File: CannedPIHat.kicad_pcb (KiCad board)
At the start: 4 copper layers, 65 x 57.2 mm, 103 parts, among them IC1 TPS56428DDA, IC2 LM1117MPX-3.3, IC3 STM32G474RET6, IC4 TJA1021TK_20_C,118, IC6 SN74LVC1G66QDCKRQ1, IC7 SN74LVC1G66QDCKRQ1, IC8 SN74LVC1G66QDCKRQ1, J1 Barrel_Jack_Switch, J2 09562627813, J5 20021511-00014T4LF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

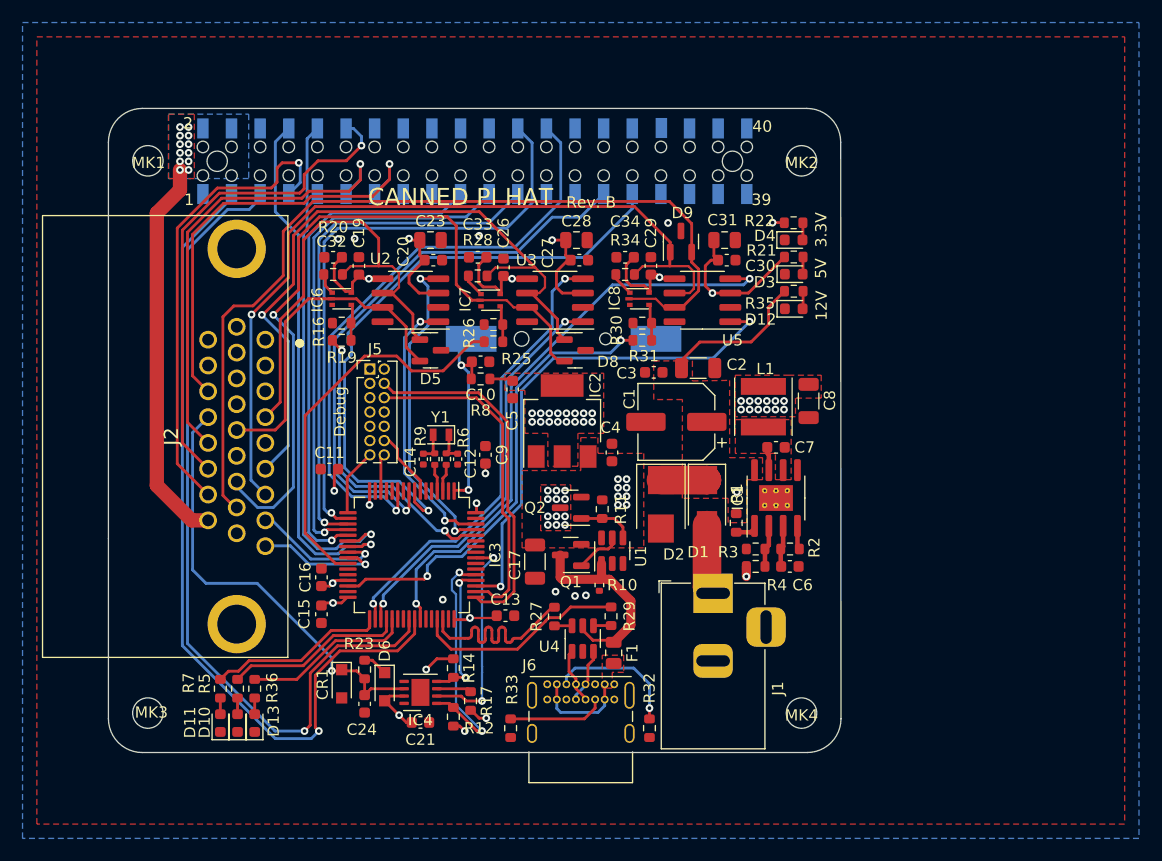
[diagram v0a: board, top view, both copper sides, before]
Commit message: Update to Rev C.
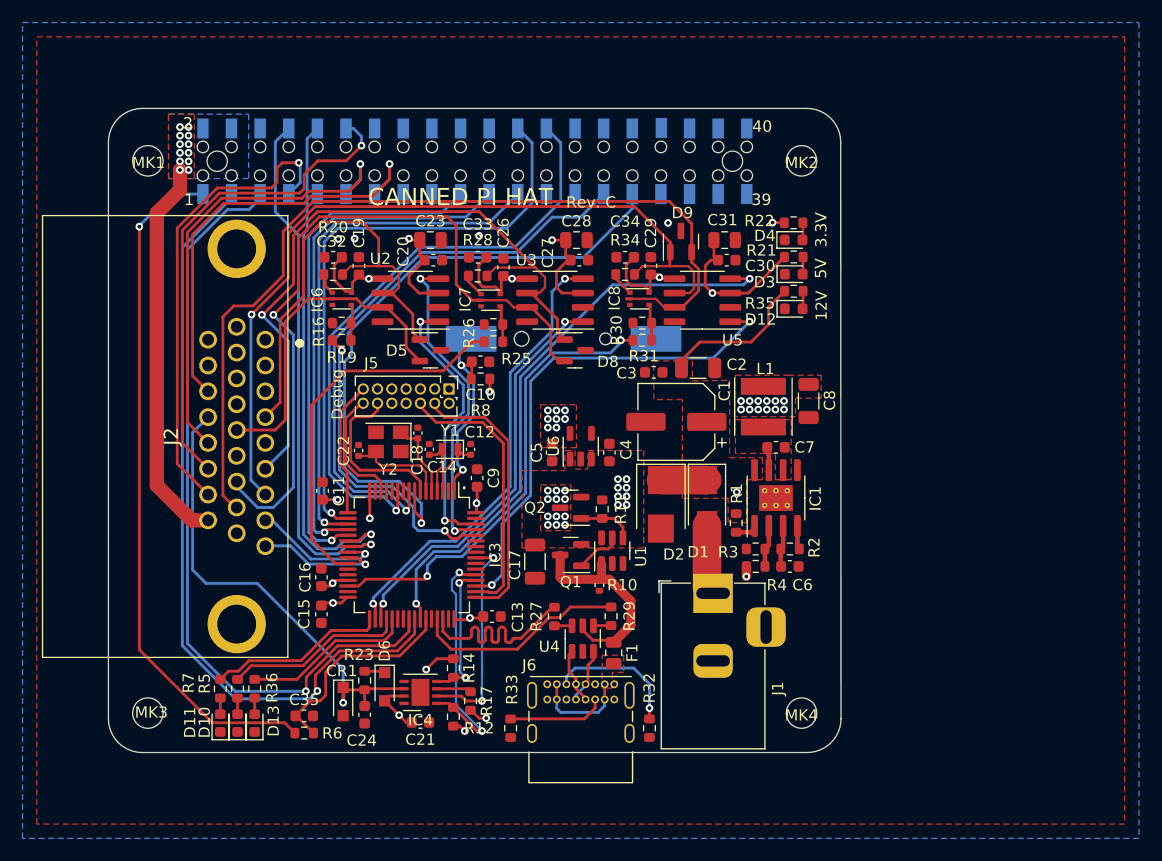
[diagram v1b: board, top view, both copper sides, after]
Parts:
- removed IC2: LM1117MPX-3.3, Package_TO_SOT_SMD:SOT-223
- removed R9: 0R, Resistor_SMD:R_0402_1005Metric
- added C18: DNP, Capacitor_SMD:C_0402_1005Metric, F.Cu at (227.5, 121.7)
- added C22: DNP, Capacitor_SMD:C_0402_1005Metric, F.Cu at (222.2, 123.2)
- added C35: 0.1uF, Capacitor_SMD:C_0603_1608Metric, F.Cu at (217.4, 146.7)
- added REF**: Symbol_Barrel_Polarity, Symbol:Symbol_Barrel_Polarity, B.Cu at (253.7, 146.6)
- added U6: AP2112K-3.3, Package_TO_SOT_SMD:SOT-23-5, F.Cu at (241.9, 122.8)
- added Y2: 8Mhz, Crystal:Crystal_SMD_3225-4Pin_3.2x2.5mm, F.Cu at (224.8, 122.4)
- C4: value 0.1uF -> 1uF
- C5: value 0.1uF -> 2uF
- R6: value 0R -> 1k; footprint Resistor_SMD:R_0402_1005Metric -> Resistor_SMD:R_0603_1608Metric
- Y1: value ECS-.327-6-12-C-TR -> 32.768Khz; footprint Crystal:Crystal_SMD_TXC_9HT11-2Pin_2.0x1.2mm -> Crystal:Crystal_SMD_2012-2Pin_2.0x1.2mm
- moved R6 27.4 mm to (217.4, 148.3), turned to 0 degrees
- moved J5 7.24 mm to (230.2, 117.7), turned to -90 degrees
- moved C5 6.60 mm to (239.4, 123.4)
- moved C9 2.19 mm to (232.7, 125.6)
- moved C11 2.02 mm to (219.0, 126.8), turned to 90 degrees
- moved CR1 1.58 mm to (220.8, 145.5)
- moved Y1 1.52 mm to (230.3, 123.1)
- moved C12 1.43 mm to (232.1, 123.1), turned to 90 degrees
- moved C13 1.20 mm to (234.0, 137.9)
- moved C14 1.02 mm to (228.5, 123.1), turned to 90 degrees
- moved R23 0.98 mm to (222.7, 143.6)
- moved C24 0.97 mm to (222.7, 146.6)
- moved C4 0.23 mm to (244.4, 123.4)
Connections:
- C12 pad 1: Net-(C12-Pad1) -> OSC32_IN
- C14 pad 1: Net-(C14-Pad1) -> OSC32_OUT
- IC3 pad 43: unconnected-(IC3-Pad43) -> RPI_SENSE
- IC3 pad 5: unconnected-(IC3-Pad5) -> OSC_IN
- IC3 pad 6: unconnected-(IC3-Pad6) -> OSC_OUT
- J5 pad 10: unconnected-(J5-Pad10) -> GND
- P1 pad 1: unconnected-(P1-Pad1) -> RPI_3.3V
- R6 pad 1: OSC32_IN -> RPI_3.3V
- R6 pad 2: Net-(C12-Pad1) -> RPI_SENSE
- Y1 pad 1: Net-(C12-Pad1) -> OSC32_IN
- Y1 pad 2: Net-(C14-Pad1) -> OSC32_OUT
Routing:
- net RPI_3.3V: track 0.00 -> 61.2 mm, vias 0 -> 1
- net RPI_SENSE: track 0.00 -> 19.1 mm
- net OSC_OUT: track 0.00 -> 9.08 mm
- net NRST: track 5.99 -> 14.7 mm
- net SYS_T_VCP_TX: track 3.26 -> 10.7 mm
- net SWDIO: track 31.5 -> 24.4 mm
- net OSC_IN: track 0.00 -> 6.91 mm
- net SYS_T_VCP_RX: track 5.96 -> 12.1 mm
- net SWCLK: track 29.7 -> 24.3 mm
- net GPIO2(SDA1): track 74.3 -> 69.2 mm
- net GPIO3(SCL1): track 74.0 -> 69.1 mm
- net OSC32_IN: track 2.38 -> 5.58 mm
- net LIN_1: track 39.2 -> 42.4 mm
- net OSC32_OUT: track 2.35 -> 5.20 mm
- net Net-(C12-Pad1): track 2.78 -> 0.00 mm
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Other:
- board text added: "+"
- board text added: "-"
- board text added: "HD DB26 Pinout 4-CAN1L 6-CAN2L 7-CAN3L 8-GPIOPB0 9-GPIOPB1 10-GND 14-CAN1H 16-CAN2H 17-CAN3H 18-3V3+ 19-VIn 21-PIGPIO27 22-LIN1 23-PIGPIO17 24-PIGPIO18 25-PIGPIO4 26-5V+"
- board text added: "Rev. C"
- board text added: "·"
- board text removed: "Rev. B"
